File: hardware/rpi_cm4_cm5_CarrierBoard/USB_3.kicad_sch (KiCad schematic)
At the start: 86 parts, among them J2 0484050003, J3 0484050003, U6 SST25VF512A, U7 UPD720202K8-711-BAA-A, U8 AP2192AFGEG-7, Y1 24MHz

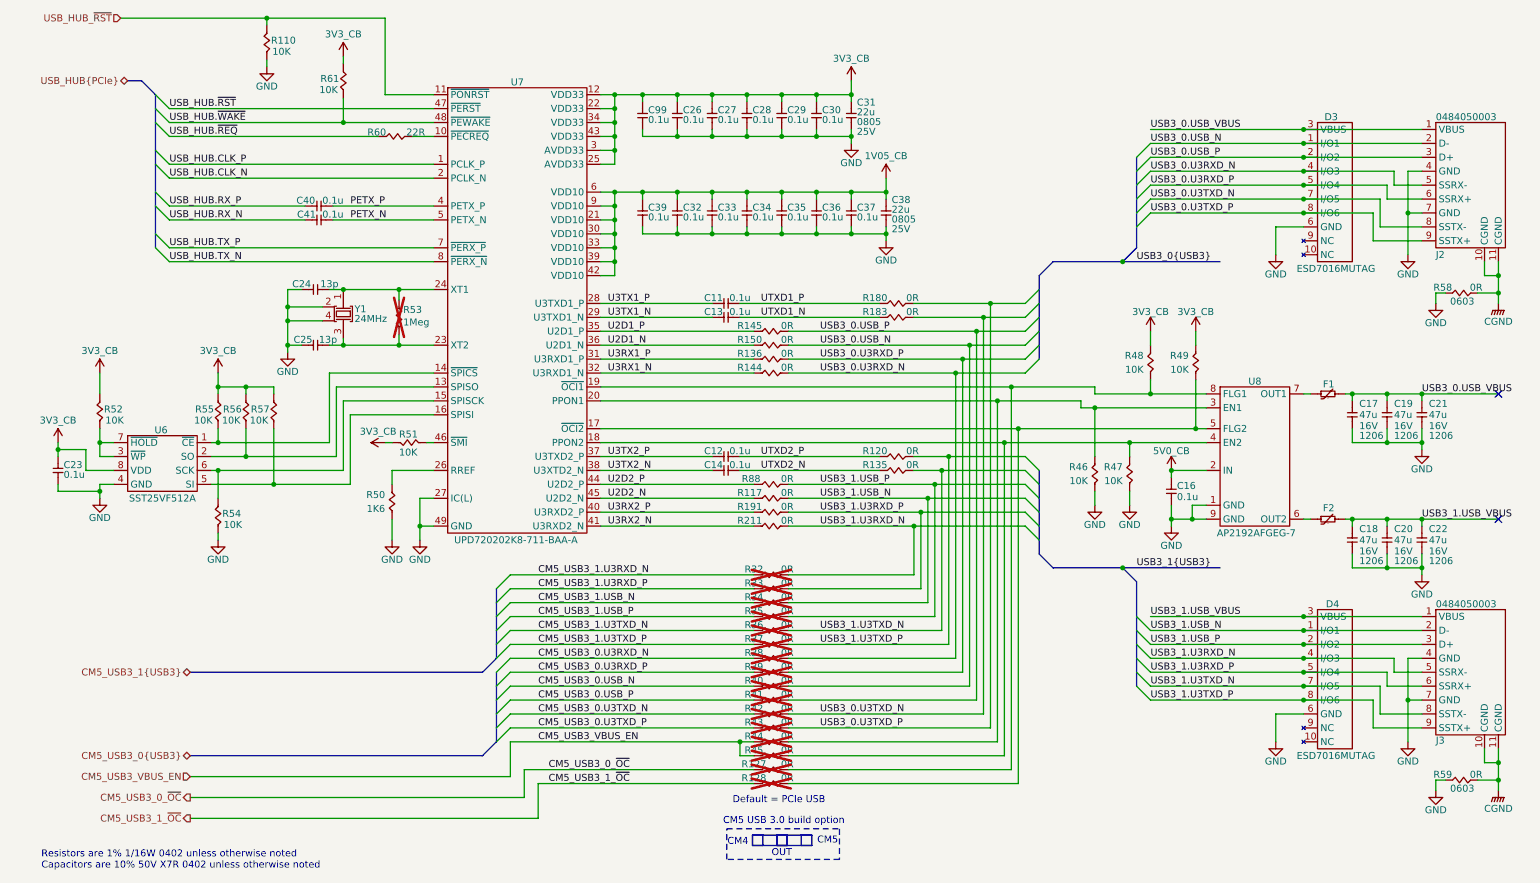
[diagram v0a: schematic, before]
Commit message: Continue working on the layout. Completed most of power planes planning and pouring Completed all DiffPairs routing and length matching (preliminary)
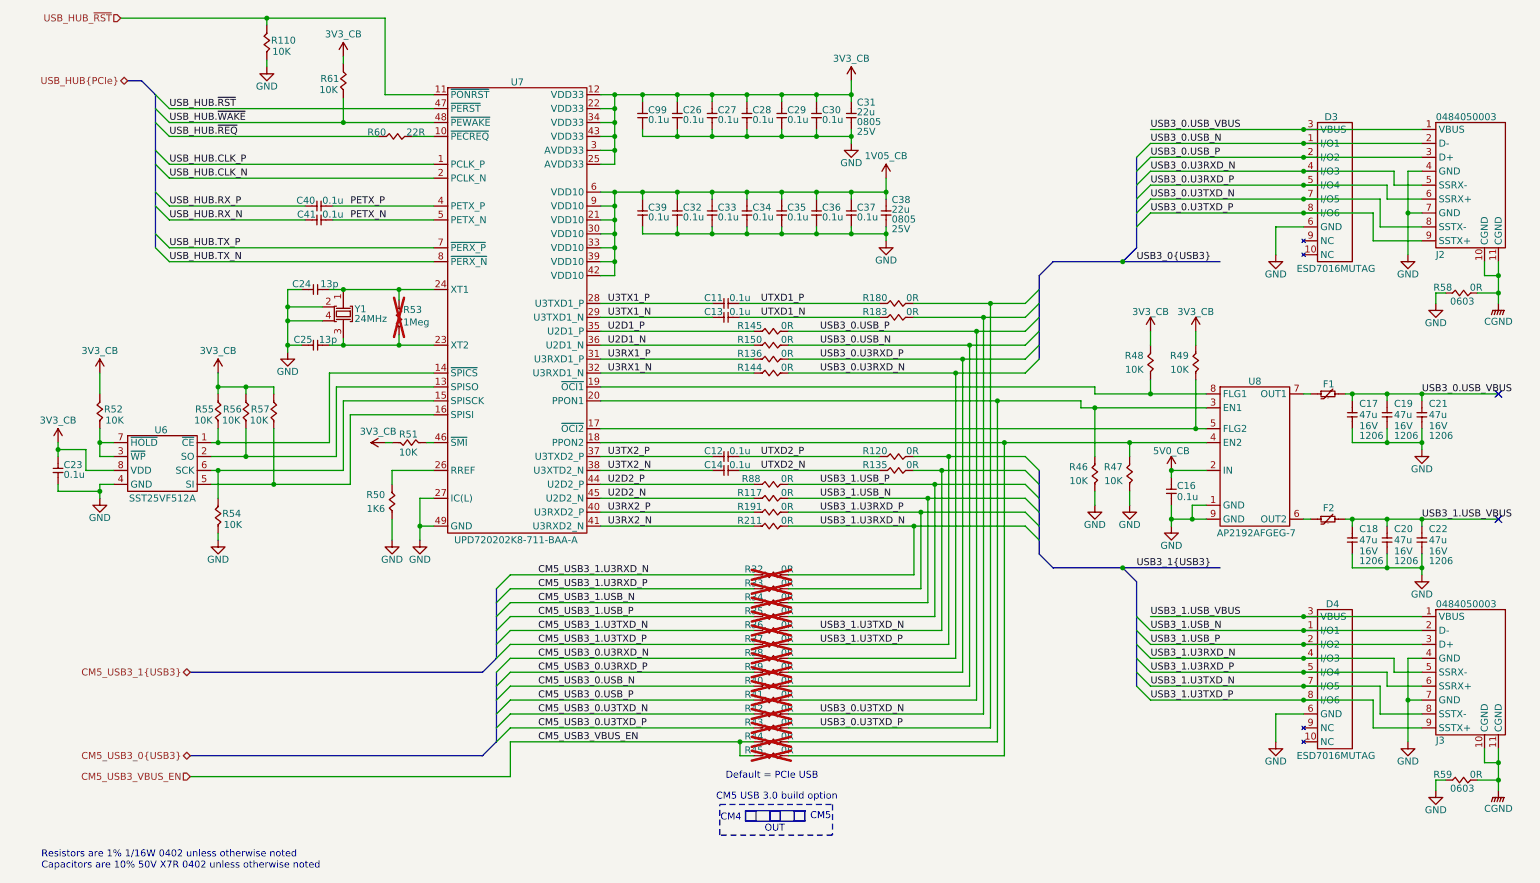
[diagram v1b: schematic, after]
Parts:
- removed R127, R128: 0R, footprint:RES_0402, symbol KicadCompDb:Resistors/RES_SMT_00001

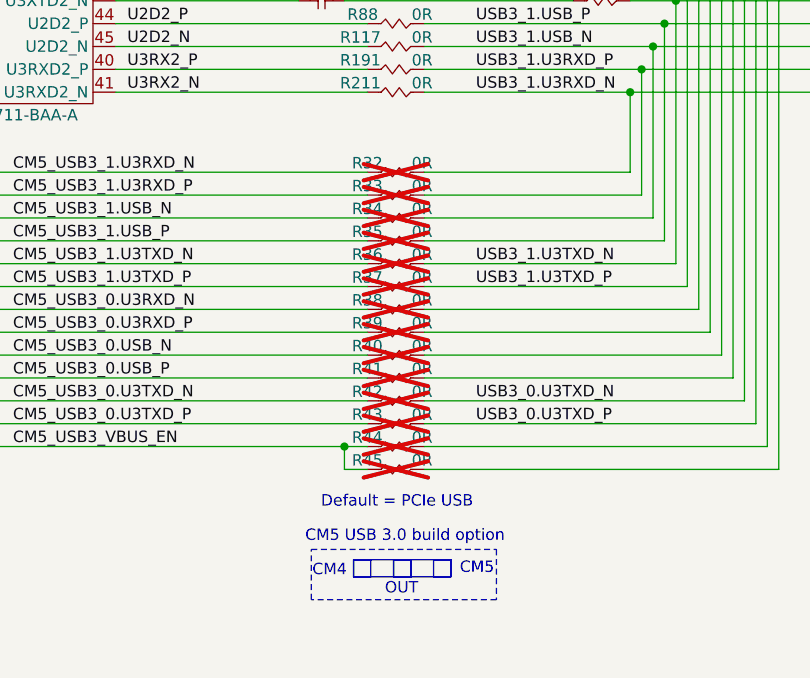
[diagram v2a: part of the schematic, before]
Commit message: Add preliminary output files (PCB PDF, Gerbers, IPC-D-356, IPC-2581, Pick_N_Place, etc) Update BOM, SCH PDF Commit PCB design and set to "Review" state
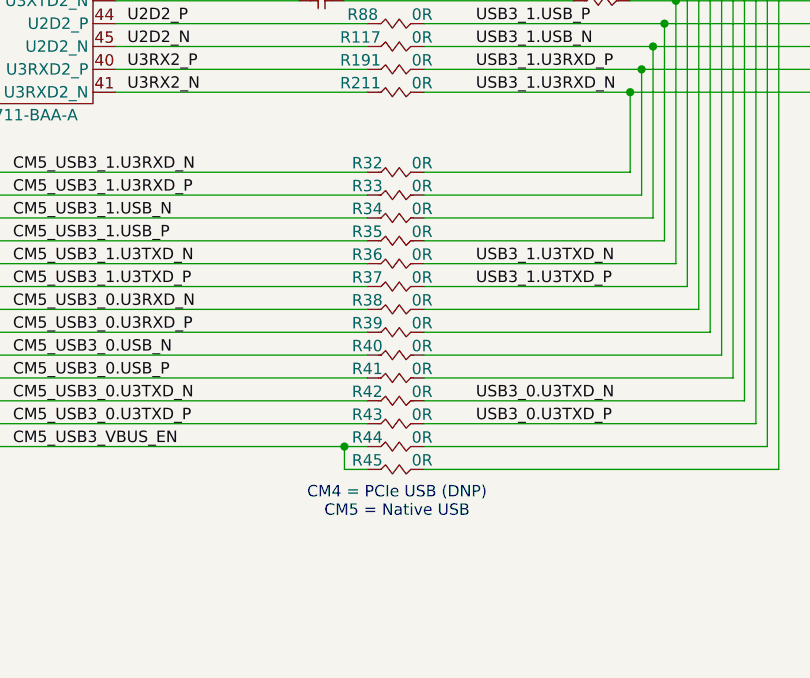
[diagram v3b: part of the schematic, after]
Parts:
- R32, R33, R34, R35, R36, R37, R38, R39, R40, R41, R42, R43, R44, R45: now fitted
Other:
- note added: "CM4 = PCIe USB (DNP) CM5 = Native USB"
- note removed: "CM4"
- note removed: "CM5"
- note removed: "CM5 USB 3.0 build option"
- note removed: "Default = PCIe USB"
- note removed: "OUT"
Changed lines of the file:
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@@
 	(title_block
 		(title "RPI CMx Carrier")
-		(date "2026-02-13")
+		(date "2026-02-15")
 		(rev "2.00-0A")
 		(comment 1 "Jean-Francois Bilodeau")
@@
 		(comment 6 "Jean-Francois Bilodeau")
 		(comment 7 "Not applicable")
-		(comment 8 "Preliminary")
+		(comment 8 "Released")
 		(comment 9 "RPI_CMx_Carrier_2.00-0A_BOM")
 	)
@@
 		)
 	)
-	(rectangle
-		(start 150.876 161.163)
-		(end 152.781 163.068)
-		(stroke
-			(width 0)
-			(type solid)
-		)
-		(fill
-			(type color)
-			(color 0 0 0 0)
-		)
-	)
-	(rectangle
-		(start 146.431 161.163)
-		(end 148.336 163.068)
-		(stroke
-			(width 0)
-			(type solid)
-		)
-		(fill
-			(type color)
-			(color 0 0 0 0)
-		)
-	)
-	(rectangle
-		(start 146.431 161.163)
-		(end 152.781 163.068)
-		(stroke
-			(width 0)
-			(type default)
-		)
-		(fill
-			(type none)
-		)
-	)
-	(rectangle
-		(start 141.986 161.163)
-		(end 143.891 163.068)
-		(stroke
-			(width 0)
-			(type solid)
-		)
-		(fill
-			(type color)
-			(color 0 0 0 0)
-		)
-	)
-	(rectangle
-		(start 137.287 160.02)
-		(end 157.861 165.608)
-		(stroke
-			(width 0)
-			(type dot)
-		)
-		(fill
-			(type none)
-		)
-	)
-	(rectangle
-		(start 141.986 161.163)
-		(end 148.336 163.068)
-		(stroke
-			(width 0)
-			(type default)
-		)
-		(fill
-			(type none)
-		)
-	)
-	(text "Default = PCIe USB"
+	(text "CM4 = PCIe USB (DNP)\nCM5 = Native USB"
 		(exclude_from_sim no)
 		(at 146.812 154.813 0)
@@
 		)
 	)
-	(text "CM4"
-		(exclude_from_sim no)
-		(at 139.319 162.433 0)
-		(effects
-			(font
-				(size 1.27 1.27)
-			)
-		)
-	)
-	(text "CM5 USB 3.0 build option"
-		(exclude_from_sim no)
-		(at 147.701 158.623 0)
-		(effects
-			(font
-				(size 1.27 1.27)
-			)
-		)
-	)
-	(text "CM5"
-		(exclude_from_sim no)
-		(at 155.702 162.179 0)
-		(effects
-			(font
-				(size 1.27 1.27)
-			)
-		)
-	)
 	(text "Resistors are 1% 1/16W 0402 unless otherwise noted\nCapacitors are 10% 50V X7R 0402 unless otherwise noted"
 		(exclude_from_sim no)
@@
 		)
 	)
-	(text "OUT"
-		(exclude_from_sim no)
-		(at 147.32 164.465 0)
-		(effects
-			(font
-				(size 1.27 1.27)
-			)
-		)
-	)
 	(junction
 		(at 118.11 35.56)
@@
 		(in_bom yes)
 		(on_board yes)
-		(dnp yes)
+		(dnp no)
 		(property "Reference" "R43"
 			(at 143.51 145.034 0)
@@
 		(in_bom yes)
 		(on_board yes)
-		(dnp yes)
+		(dnp no)
 		(property "Reference" "R38"
 			(at 143.51 132.334 0)
@@
 		(in_bom yes)
 		(on_board yes)
-		(dnp yes)
+		(dnp no)
 		(property "Reference" "R39"
 			(at 143.51 134.874 0)
@@
 		(in_bom yes)
 		(on_board yes)
-		(dnp yes)
+		(dnp no)
 		(property "Reference" "R36"
 			(at 143.51 127.254 0)
@@
 		(in_bom yes)
 		(on_board yes)
-		(dnp yes)
+		(dnp no)
 		(property "Reference" "R35"
 			(at 143.51 124.714 0)
@@
 		(in_bom yes)
 		(on_board yes)
-		(dnp yes)
+		(dnp no)
 		(property "Reference" "R42"
 			(at 143.51 142.494 0)
@@
 		(in_bom yes)
 		(on_board yes)
-		(dnp yes)
+		(dnp no)
 		(property "Reference" "R41"
 			(at 143.51 139.954 0)
@@
 		(in_bom yes)
 		(on_board yes)
-		(dnp yes)
+		(dnp no)
 		(property "Reference" "R37"
 			(at 143.51 129.794 0)
@@
 		(in_bom yes)
 		(on_board yes)
-		(dnp yes)
+		(dnp no)
 		(property "Reference" "R45"
 			(at 143.51 150.114 0)
@@
 		(in_bom yes)
 		(on_board yes)
-		(dnp yes)
+		(dnp no)
 		(property "Reference" "R44"
 			(at 143.51 147.574 0)
@@
 		(in_bom yes)
 		(on_board yes)
-		(dnp yes)
+		(dnp no)
 		(property "Reference" "R40"
 			(at 143.51 137.414 0)
@@
 		(in_bom yes)
 		(on_board yes)
-		(dnp yes)
+		(dnp no)
 		(property "Reference" "R34"
 			(at 143.51 122.174 0)
@@
 		(in_bom yes)
 		(on_board yes)
-		(dnp yes)
+		(dnp no)
 		(property "Reference" "R33"
 			(at 143.51 119.634 0)
@@
 		(in_bom yes)
 		(on_board yes)
-		(dnp yes)
+		(dnp no)
 		(property "Reference" "R32"
 			(at 143.51 117.094 0)

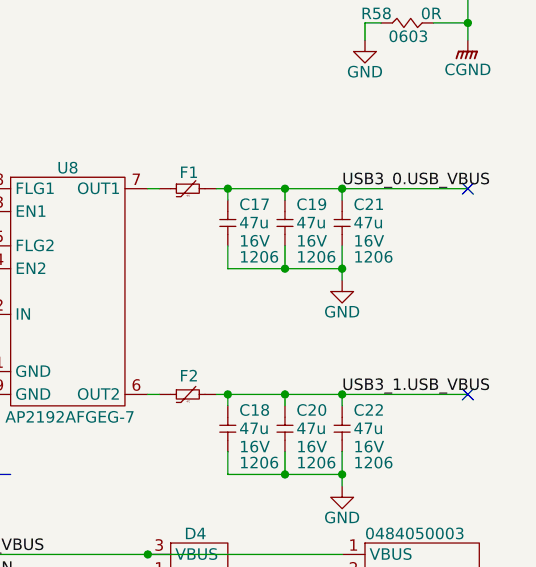
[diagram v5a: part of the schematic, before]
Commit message: Update schematic sheets (assembly variants, default cap / res notes)
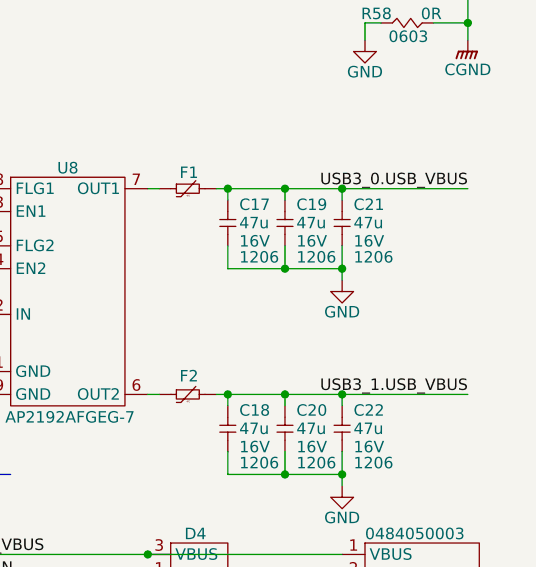
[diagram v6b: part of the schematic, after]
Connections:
- no-connect marks 2 -> 0
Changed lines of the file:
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@@
 	(title_block
 		(title "RPI CMx Carrier")
-		(date "2026-02-20")
+		(date "2026-02-22")
 		(rev "2.00-0A")
 		(comment 1 "Jean-Francois Bilodeau")
@@
 		(color 0 0 0 0)
 	)
-	(no_connect
-		(at 279.4 107.95)
-	)
-	(no_connect
-		(at 279.4 85.09)
-	)
 	(bus_entry
 		(at 96.52 148.59)
@@
 	(wire
 		(pts
-			(xy 265.43 107.95) (xy 279.4 107.95)
+			(xy 243.84 85.09) (xy 245.11 85.09)
 		)
 		(stroke
@@
 	(wire
 		(pts
-			(xy 243.84 85.09) (xy 245.11 85.09)
+			(xy 149.86 73.66) (xy 184.15 73.66)
 		)
 		(stroke
@@
 	(wire
 		(pts
-			(xy 149.86 73.66) (xy 184.15 73.66)
+			(xy 279.4 107.95) (xy 265.43 107.95)
 		)
 		(stroke
@@
 	)
 	(label "USB3_1.USB_VBUS"
-		(at 265.43 107.95 0)
+		(at 279.4 107.95 180)
 		(effects
 			(font
 				(size 1.27 1.27)
 			)
-			(justify left bottom)
+			(justify right bottom)
 		)
 	)
@@
 	)
 	(label "USB3_0.USB_VBUS"
-		(at 265.43 85.09 0)
+		(at 279.4 85.09 180)
 		(effects
 			(font
 				(size 1.27 1.27)
 			)
-			(justify left bottom)
+			(justify right bottom)
 		)
 	)
